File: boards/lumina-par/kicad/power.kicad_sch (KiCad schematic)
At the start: 19 parts, among them J3 DS1023-2*7SF11 2x7 socket 2.5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, Q101 NCE01P13K -100V P-MOSFET TO-2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, Q102 BSS123 100V N-MOSFET SOT-23

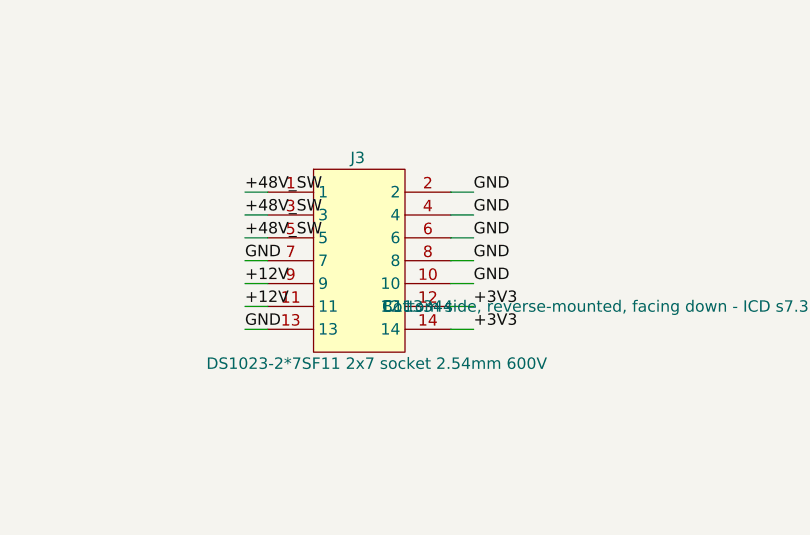
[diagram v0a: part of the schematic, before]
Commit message: ai-ee lumina-par: fix a 48V-to-GND short in the mated connector pair
The daughter reverse-mounts J3/J4 on B.Cu facing down (ICD s7.3). Flipping a
2-row connector to the back swaps its ROWS while columns stay put: measured on
the real boards, all 14 J3 pad positions coincide exactly, but carrier pin
2k+1 contacts daughter pin 2k+2.

ICD s3.1/s3.2 give ONE pin table with no mirroring instruction, and LUM-CAR-A
transcribed it literally on its top-side male header. Transcribing it literally
here too crossed 12 of 14 J3 contacts - SIX of them shorting +48V_SW straight
to GND - plus 12 live J4 crossings including ENABLE<->FAULT and the carrier's
driven DSPI_SCK onto this board's GND.

J3_PINS and J4_PINS are now the ICD tables with rows A/B exchanged, verified
pin-by-pin against lumina-carrier's own netlist: 0 crossings on both.

No gate in the pipeline could see this - erc 0/0 and netlist_audit exit 0
throughout - because every check compares a board against itself.

Also: P5 re-run (stackup -3313 is a phantom, now JLC04161H-1080B), parity 6->0
via in_bom on the non-BOM parts, ICD s7.2 re-issued from the carrier's actual
placement (+7.970 mm in Y), constraints translated per stackup.md TRAP 2, and
the 0.635 mm HV clearance re-applied after rules_gen overwrote it.

Co-Authored-By: Claude Opus 5 (1M context) <noreply@anthropic.com>
Claude-Session: https://claude.ai/code/session_01UFFGtZjuFWQS5j9Bw2cwpp
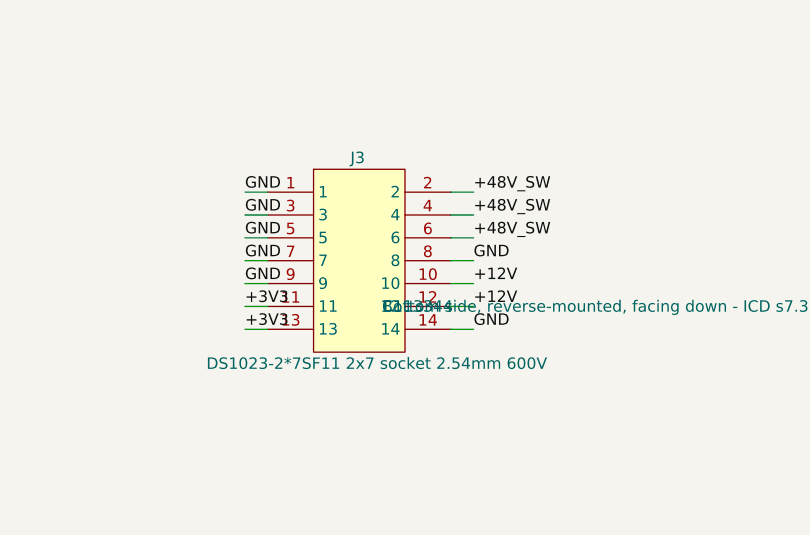
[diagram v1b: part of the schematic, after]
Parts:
- H5, TP101, TP102, TP103: now left out of the parts list
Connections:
- net +12V: now also J3.10, J3.12; no longer J3.11, J3.9
- net +3V3: now also J3.11, J3.13; no longer J3.12, J3.14
- net +48V_SW: now also J3.2, J3.4, J3.6; no longer J3.1, J3.3, J3.5
- net GND: now also J3.1, J3.14, J3.3, J3.5, J3.9; no longer J3.10, J3.13, J3.2, J3.4, J3.6
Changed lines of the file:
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@@
 		(instances
 			(project "power"
-				(path "/3c352d5f-91fc-4442-af5d-f2f38349da74"
+				(path "/3f337d63-8bb2-4204-9f0a-501408ec2a89"
 					(reference "J3")
 					(unit 1)
@@
 		(instances
 			(project "power"
-				(path "/3c352d5f-91fc-4442-af5d-f2f38349da74"
+				(path "/3f337d63-8bb2-4204-9f0a-501408ec2a89"
 					(reference "#PWR100")
 					(unit 1)
@@
 		(instances
 			(project "power"
-				(path "/3c352d5f-91fc-4442-af5d-f2f38349da74"
+				(path "/3f337d63-8bb2-4204-9f0a-501408ec2a89"
 					(reference "#FLG100")
 					(unit 1)
@@
 		(instances
 			(project "power"
-				(path "/3c352d5f-91fc-4442-af5d-f2f38349da74"
+				(path "/3f337d63-8bb2-4204-9f0a-501408ec2a89"
 					(reference "#PWR101")
 					(unit 1)
@@
 		(instances
 			(project "power"
-				(path "/3c352d5f-91fc-4442-af5d-f2f38349da74"
+				(path "/3f337d63-8bb2-4204-9f0a-501408ec2a89"
 					(reference "#FLG101")
 					(unit 1)
@@
 		(instances
 			(project "power"
-				(path "/3c352d5f-91fc-4442-af5d-f2f38349da74"
+				(path "/3f337d63-8bb2-4204-9f0a-501408ec2a89"
 					(reference "#PWR102")
 					(unit 1)
@@
 		(instances
 			(project "power"
-				(path "/3c352d5f-91fc-4442-af5d-f2f38349da74"
+				(path "/3f337d63-8bb2-4204-9f0a-501408ec2a89"
 					(reference "#FLG102")
 					(unit 1)
@@
 		(instances
 			(project "power"
-				(path "/3c352d5f-91fc-4442-af5d-f2f38349da74"
+				(path "/3f337d63-8bb2-4204-9f0a-501408ec2a89"
 					(reference "#PWR103")
 					(unit 1)
@@
 		(instances
 			(project "power"
-				(path "/3c352d5f-91fc-4442-af5d-f2f38349da74"
+				(path "/3f337d63-8bb2-4204-9f0a-501408ec2a89"
 					(reference "#FLG103")
 					(unit 1)
@@
 		(unit 1)
 		(exclude_from_sim no)
-		(in_bom yes)
+		(in_bom no)
 		(on_board yes)
 		(dnp no)
@@
 		(instances
 			(project "power"
-				(path "/3c352d5f-91fc-4442-af5d-f2f38349da74"
+				(path "/3f337d63-8bb2-4204-9f0a-501408ec2a89"
 					(reference "TP101")
 					(unit 1)
@@
 		(unit 1)
 		(exclude_from_sim no)
-		(in_bom yes)
+		(in_bom no)
 		(on_board yes)
 		(dnp no)
@@
 		(instances
 			(project "power"
-				(path "/3c352d5f-91fc-4442-af5d-f2f38349da74"
+				(path "/3f337d63-8bb2-4204-9f0a-501408ec2a89"
 					(reference "TP102")
 					(unit 1)
@@
 		(unit 1)
 		(exclude_from_sim no)
-		(in_bom yes)
+		(in_bom no)
 		(on_board yes)
 		(dnp no)
@@
 		(instances
 			(project "power"
-				(path "/3c352d5f-91fc-4442-af5d-f2f38349da74"
+				(path "/3f337d63-8bb2-4204-9f0a-501408ec2a89"
 					(reference "TP103")
 					(unit 1)
@@
 		(unit 1)
 		(exclude_from_sim no)
-		(in_bom yes)
+		(in_bom no)
 		(on_board yes)
 		(dnp no)
@@
 		(instances
 			(project "power"
-				(path "/3c352d5f-91fc-4442-af5d-f2f38349da74"
+				(path "/3f337d63-8bb2-4204-9f0a-501408ec2a89"
 					(reference "H5")
 					(unit 1)
@@
 		(instances
 			(project "power"
-				(path "/3c352d5f-91fc-4442-af5d-f2f38349da74"
+				(path "/3f337d63-8bb2-4204-9f0a-501408ec2a89"
 					(reference "C101")
 					(unit 1)
@@
 		(instances
 			(project "power"
-				(path "/3c352d5f-91fc-4442-af5d-f2f38349da74"
+				(path "/3f337d63-8bb2-4204-9f0a-501408ec2a89"
 					(reference "C102")
 					(unit 1)
@@
 		(instances
 			(project "power"
-				(path "/3c352d5f-91fc-4442-af5d-f2f38349da74"
+				(path "/3f337d63-8bb2-4204-9f0a-501408ec2a89"
 					(reference "C103")
 					(unit 1)
@@
 		(instances
 			(project "power"
-				(path "/3c352d5f-91fc-4442-af5d-f2f38349da74"
+				(path "/3f337d63-8bb2-4204-9f0a-501408ec2a89"
 					(reference "C104")
 					(unit 1)
@@
 		(instances
 			(project "power"
-				(path "/3c352d5f-91fc-4442-af5d-f2f38349da74"
+				(path "/3f337d63-8bb2-4204-9f0a-501408ec2a89"
 					(reference "C105")
 					(unit 1)
@@
 		(instances
 			(project "power"
-				(path "/3c352d5f-91fc-4442-af5d-f2f38349da74"
+				(path "/3f337d63-8bb2-4204-9f0a-501408ec2a89"
 					(reference "R101")
 					(unit 1)
@@
 		(instances
 			(project "power"
-				(path "/3c352d5f-91fc-4442-af5d-f2f38349da74"
+				(path "/3f337d63-8bb2-4204-9f0a-501408ec2a89"
 					(reference "Q101")
 					(unit 1)
@@
 		(instances
 			(project "power"
-				(path "/3c352d5f-91fc-4442-af5d-f2f38349da74"
+				(path "/3f337d63-8bb2-4204-9f0a-501408ec2a89"
 					(reference "C108")
 					(unit 1)
@@
 		(instances
 			(project "power"
-				(path "/3c352d5f-91fc-4442-af5d-f2f38349da74"
+				(path "/3f337d63-8bb2-4204-9f0a-501408ec2a89"
 					(reference "C106")
 					(unit 1)
@@
 		(instances
 			(project "power"
-				(path "/3c352d5f-91fc-4442-af5d-f2f38349da74"
+				(path "/3f337d63-8bb2-4204-9f0a-501408ec2a89"
 					(reference "C107")
 					(unit 1)
@@
 		(instances
 			(project "power"
-				(path "/3c352d5f-91fc-4442-af5d-f2f38349da74"
+				(path "/3f337d63-8bb2-4204-9f0a-501408ec2a89"
 					(reference "R103")
 					(unit 1)
@@
 		(instances
 			(project "power"
-				(path "/3c352d5f-91fc-4442-af5d-f2f38349da74"
+				(path "/3f337d63-8bb2-4204-9f0a-501408ec2a89"
 					(reference "R102")
 					(unit 1)
@@
 		(instances
 			(project "power"
-				(path "/3c352d5f-91fc-4442-af5d-f2f38349da74"
+				(path "/3f337d63-8bb2-4204-9f0a-501408ec2a89"
 					(reference "Q102")
 					(unit 1)
@@
 		(instances
 			(project "power"
-				(path "/3c352d5f-91fc-4442-af5d-f2f38349da74"
+				(path "/3f337d63-8bb2-4204-9f0a-501408ec2a89"
 					(reference "R104")
 					(unit 1)
@@
 		)
 	)
-	(label "+48V_SW"
+	(label "GND"
 		(at 50.8 68.58 0.0000)
 		(effects
@@
 		)
 	)
-	(label "GND"
+	(label "+12V"
 		(at 76.2 78.74 0.0000)
 		(effects
@@
 		)
 	)
-	(label "+12V"
+	(label "+3V3"
 		(at 50.8 81.28 0.0000)
 		(effects
@@
 		)
 	)
-	(label "+3V3"
+	(label "+12V"
 		(at 76.2 81.28 0.0000)
 		(effects
@@
 		)
 	)
-	(label "GND"
+	(label "+3V3"
 		(at 50.8 83.82 0.0000)
 		(effects
@@
 		)
 	)
-	(label "+3V3"
+	(label "GND"
 		(at 76.2 83.82 0.0000)
 		(effects
@@
 		)
 	)
-	(label "GND"
+	(label "+48V_SW"
 		(at 76.2 68.58 0.0000)
 		(effects
@@
 		)
 	)
-	(label "+48V_SW"
+	(label "GND"
 		(at 50.8 71.12 0.0000)
 		(effects
@@
 		)
 	)
-	(label "GND"
+	(label "+48V_SW"
 		(at 76.2 71.12 0.0000)
 		(effects
@@
 		)
 	)
-	(label "+48V_SW"
+	(label "GND"
 		(at 50.8 73.66 0.0000)
 		(effects
@@
 		)
 	)
-	(label "GND"
+	(label "+48V_SW"
 		(at 76.2 73.66 0.0000)
 		(effects
@@
 		)
 	)
-	(label "+12V"
+	(label "GND"
 		(at 50.8 78.74 0.0000)
 		(effects
